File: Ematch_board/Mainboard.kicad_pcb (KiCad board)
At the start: 4 copper layers, 57.3 x 53.3 mm, 128 parts, among them J1 Conn_01x02_Male, J10 Conn_01x02_Male, J2 Conn_01x02_Male, J3 Conn_01x02_Male, J4 Conn_01x02_Male, J5 Conn_01x02_Male, J6 Conn_01x02_Male, J7 Conn_01x06_Female, J8 USB_C_Receptacle_USB2.0, J9 Conn_01x02_Male, Q1 MMDT2222A, Q51 PMV20ENR, Q52 PMV20ENR, Q53 PMV20ENR, Q54 PMV20ENR, Q55 PMV20ENR, Q56 PMV20ENR, U1 LTV-247, U2 LTC4411, U3 RT9025-25GSP, U4 LTC4411, U5 SN65HVD230, U6 CP2102-GMR-QFN28

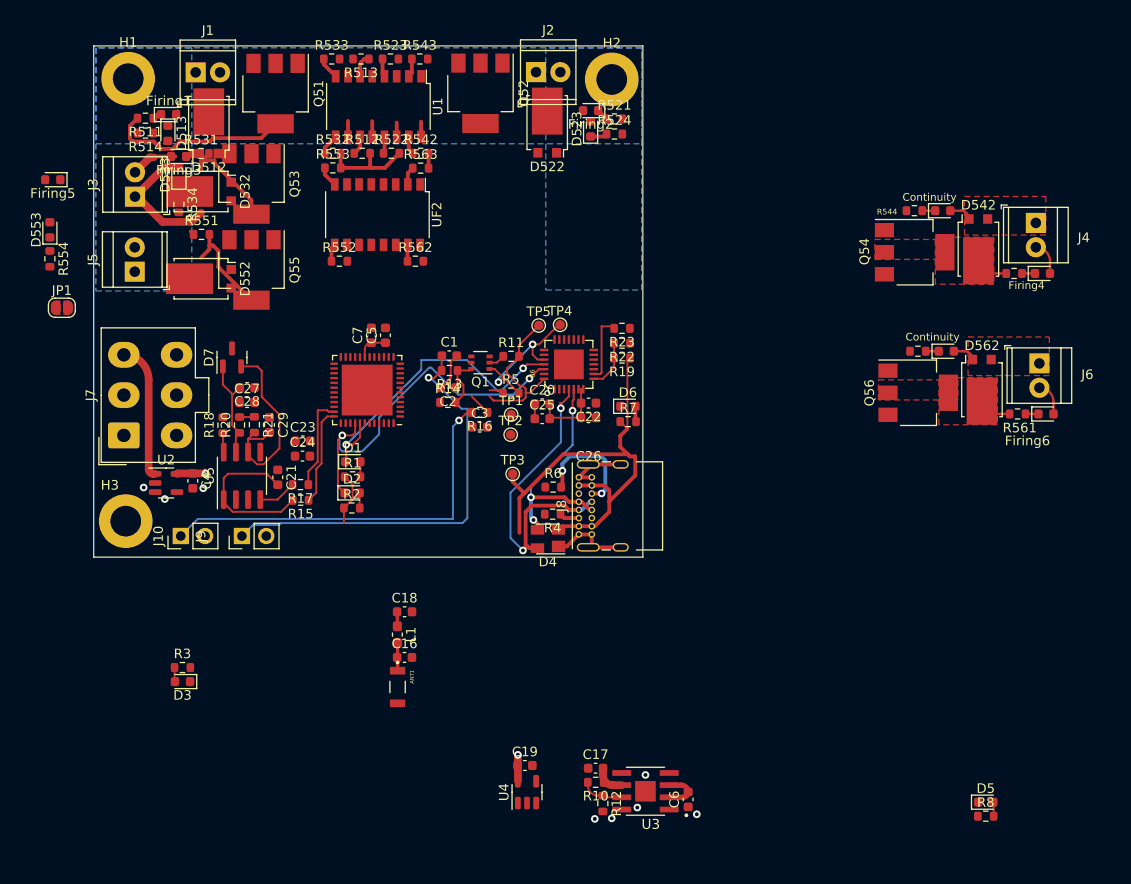
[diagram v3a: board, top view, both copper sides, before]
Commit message: completed layout for screw terminals, moved some LEDs
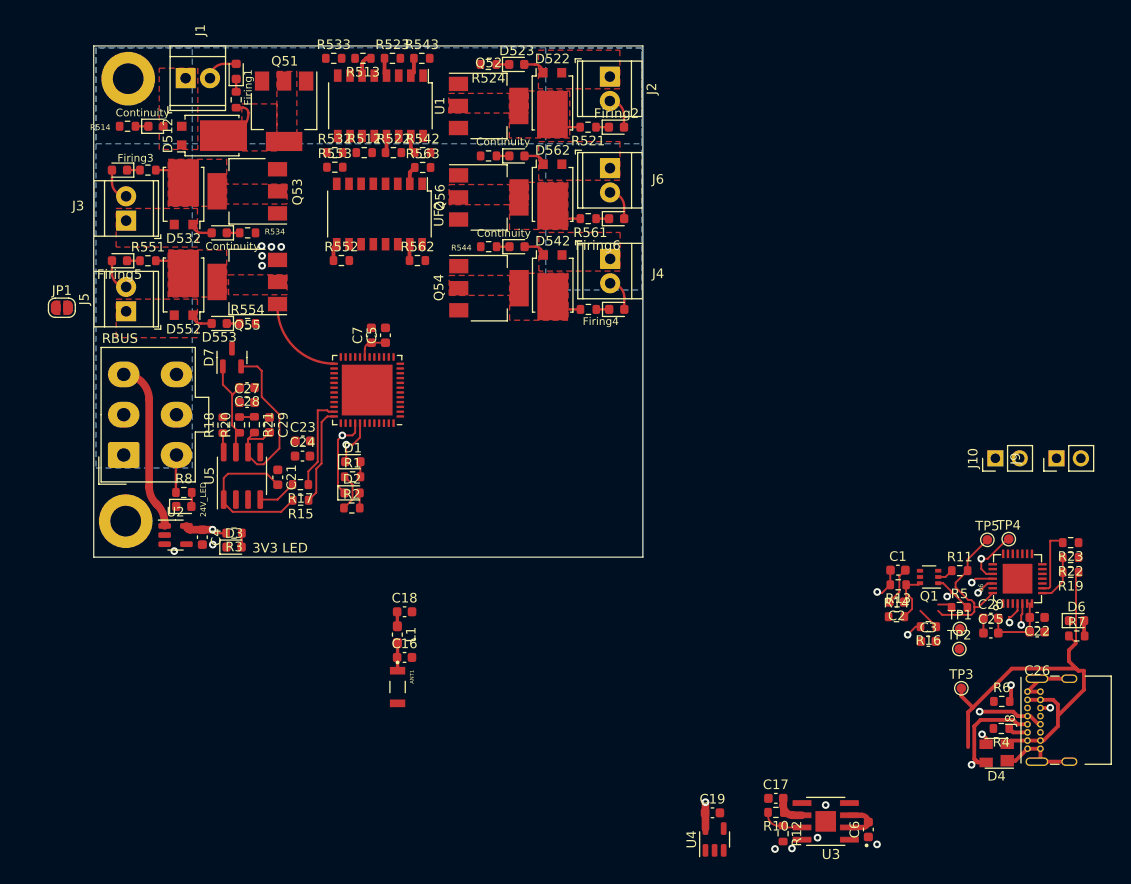
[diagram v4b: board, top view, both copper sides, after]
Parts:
- removed H2: MountingHole_Pad, MountingHole:MountingHole_3.2mm_M3_DIN965_Pad
- D3: value PWR_LED -> 3V3 LED
- J7: value Conn_01x06_Female -> RBUS
- moved R8 90.2 mm to (127.4, 116.1)
- moved D5 89.1 mm to (127.4, 117.5)
- moved J9 85.3 mm to (218.4, 112.5)
- moved J10 85.3 mm to (212.0, 112.5)
- moved D6 51.8 mm to (220.4, 129.4)
- moved R16 51.8 mm to (205.0, 130.1)
- moved R22 51.8 mm to (219.8, 122.8)
- moved R4 51.8 mm to (212.6, 140.7)
- moved C1 51.8 mm to (201.8, 124.2)
- moved C3 51.8 mm to (205.0, 131.6)
- moved Q1 51.8 mm to (205.1, 124.9)
- moved R14 51.8 mm to (201.7, 129.0)
- moved R19 51.8 mm to (219.8, 124.4)
- moved R23 51.8 mm to (219.8, 121.3)
- moved TP2 51.8 mm to (208.2, 132.4)
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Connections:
- D522 pad 3: Net-(D522-Pad3) -> unconnected-(D522-Pad3)
- Firing1 pad 2: /24V -> +24V
- Firing2 pad 2: /24V -> +24V
- Firing3 pad 2: /24V -> +24V
- Firing4 pad 2: /24V -> +24V
- Firing5 pad 2: /24V -> +24V
- Firing6 pad 2: /24V -> +24V
- J1 pad 2: /24V -> +24V
- J2 pad 2: /24V -> +24V
- J3 pad 2: /24V -> +24V
- J4 pad 2: /24V -> +24V
- J5 pad 2: /24V -> +24V
- J6 pad 2: /24V -> +24V
- Q51 pad 1: /ematch/Nuke 1 -> /Nuke 1
- Q52 pad 1: /ematch/Nuke 2 -> /Nuke 2
- Q52 pad 2: Net-(D522-Pad3) -> Net-(Q52-Pad2)
- Q52 pad 4: Net-(D522-Pad3) -> Net-(Q52-Pad2)
- Q53 pad 1: /ematch/Nuke 3 -> /Nuke 3
- Q54 pad 1: /ematch/Nuke 4 -> /Nuke 4
- Q55 pad 1: /ematch/Nuke 5 -> /Nuke 5
- Q56 pad 1: /ematch/Nuke 6 -> /Nuke 6
- R512 pad 1: /ematch/Cont1 -> /Cont 1
- R521 pad 2: Net-(D522-Pad3) -> Net-(Q52-Pad2)
- R522 pad 1: /ematch/Cont2 -> /Cont 2
- R532 pad 1: /ematch/Cont3 -> /Cont 3
- R542 pad 1: /ematch/Cont4 -> /Cont 4
- R552 pad 1: /ematch/Cont5 -> /Cont 5
- R562 pad 1: /ematch/Cont6 -> /Cont 6
- U1 pad 11: /ematch/Cont1 -> /Cont 1
- U1 pad 13: /ematch/Cont2 -> /Cont 2
- U1 pad 15: /ematch/Cont4 -> /Cont 4
- U1 pad 9: /ematch/Cont3 -> /Cont 3
- UF2 pad 15: /ematch/Cont6 -> /Cont 6
- UF2 pad 9: /ematch/Cont5 -> /Cont 5
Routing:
- net Net-(C1-Pad1): track 43.6 -> 2.86 mm
- net Net-(C3-Pad1): track 41.3 -> 1.68 mm
- net /TXD: track 38.8 -> 11.3 mm
- net +24V: track 0.00 -> 25.0 mm
- net /RXD: track 32.3 -> 7.27 mm
- net /Data+: track 33.2 -> 14.0 mm
- net Net-(D512-Pad3): track 19.2 -> 5.42 mm
- net /Data-: track 23.7 -> 10.4 mm
- net /24V: track 12.6 -> 0.00 mm
- net Net-(D532-Pad1): track 14.0 -> 2.42 mm
- net GND: track 32.3 -> 20.9 mm, vias 8 -> 12
- net Net-(Firing3-Pad1): track 11.0 -> 1.35 mm
- net /Nuke 5: track 0.00 -> 9.35 mm
- net Net-(J8-PadB5): track 11.9 -> 2.59 mm
- net Net-(D552-Pad3): track 10.5 -> 3.60 mm
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- added copper zone on B.Cu, net +24V
- added copper zone on F.Cu, net Net-(D512-Pad1)
- added copper zone on F.Cu, net Net-(D512-Pad3)
- added copper zone on F.Cu, net Net-(D522-Pad1)
- added copper zone on F.Cu, net Net-(D532-Pad1)
- added copper zone on F.Cu, net Net-(D532-Pad3)
- added copper zone on F.Cu, net Net-(D552-Pad1)
- added copper zone on F.Cu, net Net-(D552-Pad3)
- added copper zone on F.Cu, net Net-(Q52-Pad2)
- removed copper zone on B.Cu, net /24V

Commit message: initial routing of cont and nuke traces
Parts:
- added H2: MountingHole_Pad, MountingHole:MountingHole_3.2mm_M3_DIN965_Pad, F.Cu at (171.3, 119.0)
- D3: value 3V3 LED -> PWR_LED
- moved R563 3.28 mm to (150.1, 84.6), turned to 180 degrees
- moved R553 2.64 mm to (144.2, 84.6)
- moved R562 2.35 mm to (151.8, 94.2)
- moved UF2 2.35 mm to (147.9, 89.4)
- moved R552 2.31 mm to (144.2, 94.2)
- moved R532 0.80 mm to (143.9, 80.5)
- moved R512 0.68 mm to (146.8, 80.5)
- moved R522 0.59 mm to (149.8, 80.5)
- moved R542 0.50 mm to (152.8, 80.5)
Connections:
- GND1 pad 12: /Nuke 1 -> unconnected-(GND1-Pad12)
- GND1 pad 17: /Cont 4 -> unconnected-(GND1-Pad17)
- GND1 pad 18: /Cont 2 -> unconnected-(GND1-Pad18)
- GND1 pad 20: /Cont 1 -> unconnected-(GND1-Pad20)
- GND1 pad 22: /Cont 3 -> unconnected-(GND1-Pad22)
- GND1 pad 24: /Nuke 3 -> unconnected-(GND1-Pad24)
- GND1 pad 25: /Nuke 5 -> unconnected-(GND1-Pad25)
- GND1 pad 28: unconnected-(GND1-Pad28) -> /Cont 4
- GND1 pad 29: unconnected-(GND1-Pad29) -> /Cont 2
- GND1 pad 30: unconnected-(GND1-Pad30) -> /Cont 1
- GND1 pad 31: unconnected-(GND1-Pad31) -> /Cont 3
- GND1 pad 32: unconnected-(GND1-Pad32) -> /Nuke 1
- GND1 pad 33: unconnected-(GND1-Pad33) -> /Nuke 3
- GND1 pad 34: unconnected-(GND1-Pad34) -> /Nuke 5
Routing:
- net /Nuke 1: track 0.00 -> 35.2 mm
- net /Cont 4: track 1.90 -> 33.8 mm
- net /Cont 2: track 1.62 -> 32.3 mm
- net /Cont 1: track 0.00 -> 30.4 mm
- net /Cont 3: track 0.00 -> 29.8 mm
- net /Nuke 3: track 0.00 -> 29.5 mm
- net /Nuke 2: track 0.00 -> 24.3 mm
- net /Nuke 6: track 0.00 -> 14.4 mm
- net +3V3: track 22.9 -> 37.2 mm, vias 2 -> 3
- net /Nuke 4: track 0.00 -> 8.43 mm
- net /Nuke 5: track 9.35 -> 14.0 mm
- net /Cont 5: track 1.84 -> 4.75 mm
- net Net-(R563-Pad1): track 1.91 -> 0.00 mm
- net Net-(R553-Pad1): track 0.00 -> 1.69 mm
- net /CAN_RX: track 9.92 -> 9.26 mm
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
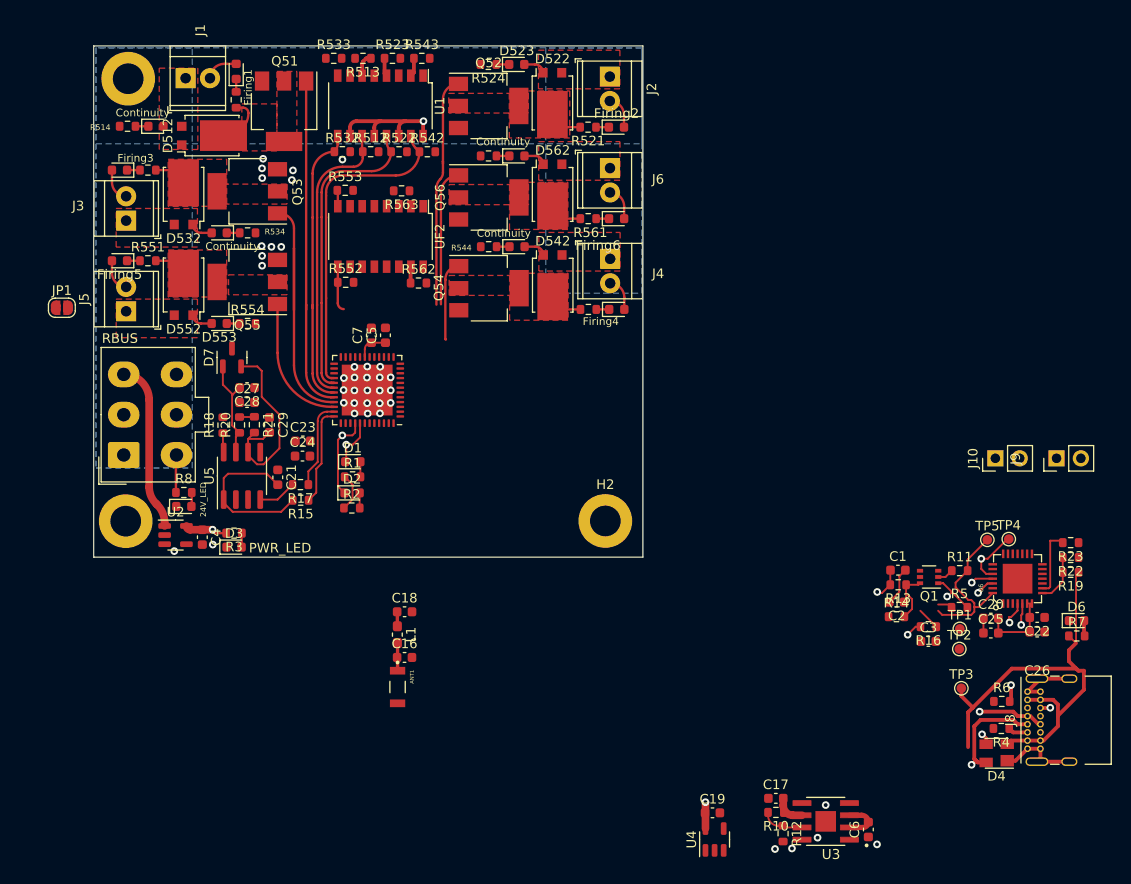
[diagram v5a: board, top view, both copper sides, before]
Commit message: completed routing, changed antenna for U.FL connector
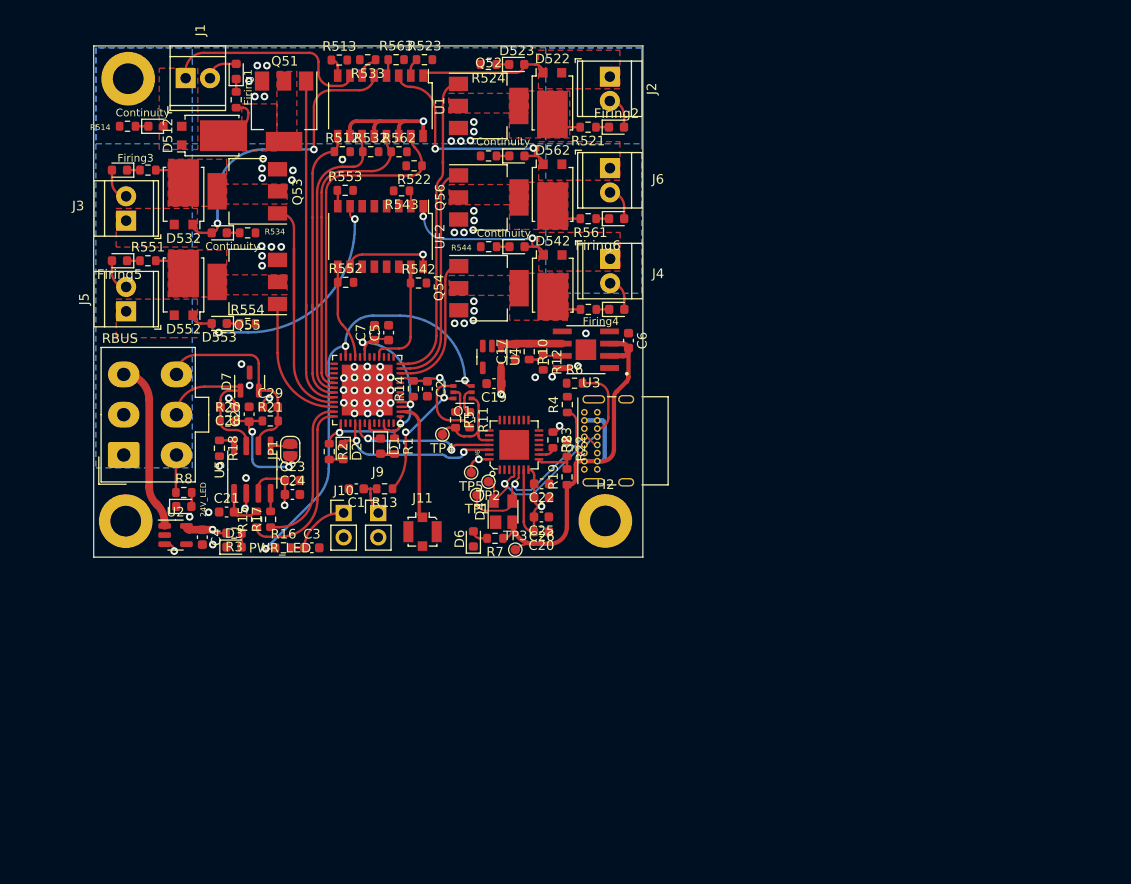
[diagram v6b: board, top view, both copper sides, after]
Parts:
- removed ANT1: AMCA31-2R450G-S1F-T3, iclr:ANT_AMCA31-2R450G-S1F-T3
- removed C16: 33pF, Capacitor_SMD:C_0603_1608Metric
- removed C18: 100pF, Capacitor_SMD:C_0603_1608Metric
- removed L1: LQG15WZ1N8B02D, Inductor_SMD:L_0603_1608Metric_Pad1.05x0.95mm_HandSolder
- added J11: Conn_Coaxial, Connector_Coaxial:U.FL_Molex_MCRF_73412-0110_Vertical, F.Cu at (152.2, 120.2)
- moved J9 70.9 mm to (147.6, 118.2), turned to 0 degrees
- moved J10 68.2 mm to (144.0, 118.2), turned to 0 degrees
- moved R16 67.7 mm to (137.8, 121.8), turned to 0 degrees
- moved C3 65.0 mm to (140.7, 121.8)
- moved D6 63.5 mm to (157.6, 120.9), turned to 90 degrees
- moved R7 61.5 mm to (159.8, 120.8), turned to 180 degrees
- moved TP4 60.1 mm to (154.3, 110.0), turned to 180 degrees
- moved D4 57.3 mm to (160.6, 118.1), turned to 90 degrees
- moved C1 57.1 mm to (145.3, 115.7), turned to 180 degrees
- moved C6 56.8 mm to (173.7, 100.2), turned to -90 degrees
- moved R4 56.5 mm to (167.3, 106.9), turned to 90 degrees
- moved R5 56.1 mm to (155.7, 108.5), turned to -90 degrees
- moved R14 55.7 mm to (151.3, 105.2), turned to 90 degrees
- moved R6 55.5 mm to (168.1, 104.7)
- moved U4 55.4 mm to (159.5, 101.9), turned to -90 degrees
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- renumbered R532 to R512, R533 to R513, R542 to R522, R543 to R523, R512 to R532, R513 to R533, R562 to R542, R563 to R543, R522 to R562, R523 to R563
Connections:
- GND1 pad 10: unconnected-(GND1-Pad10) -> /Nuke 4
- GND1 pad 11: unconnected-(GND1-Pad11) -> /Nuke 6
- GND1 pad 12: unconnected-(GND1-Pad12) -> /Nuke 2
- GND1 pad 13: /Nuke 6 -> unconnected-(GND1-Pad13)
- GND1 pad 14: /Nuke 4 -> unconnected-(GND1-Pad14)
- GND1 pad 15: /Nuke 2 -> unconnected-(GND1-Pad15)
- GND1 pad 16: /Cont 6 -> /Cont 4
- GND1 pad 28: /Cont 4 -> /Cont 2
- GND1 pad 29: /Cont 2 -> /Cont 6
- GND1 pad 30: /Cont 1 -> /Cont 3
- GND1 pad 31: /Cont 3 -> /Cont 1
- R512 pad 1: /Cont 3 -> /Cont 1
- R522 pad 1: /Cont 4 -> /Cont 2
- R532 pad 1: /Cont 1 -> /Cont 3
- R542 pad 1: /Cont 6 -> /Cont 4
- R562 pad 1: /Cont 2 -> /Cont 6
- U1 pad 1: Net-(D542-Pad1) -> Net-(D522-Pad1)
- U1 pad 11: /Cont 1 -> /Cont 3
- U1 pad 13: /Cont 2 -> /Cont 6
- U1 pad 15: /Cont 4 -> /Cont 2
- U1 pad 3: Net-(D522-Pad1) -> Net-(D562-Pad1)
- U1 pad 5: Net-(D512-Pad1) -> Net-(D532-Pad1)
- U1 pad 7: Net-(D532-Pad1) -> Net-(D512-Pad1)
- U1 pad 9: /Cont 3 -> /Cont 1
- UF2 pad 1: Net-(D562-Pad1) -> Net-(D542-Pad1)
- UF2 pad 15: /Cont 6 -> /Cont 4
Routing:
- net +3V3: track 37.2 -> 90.2 mm, vias 3 -> 11
- net /BOOT: track 2.35 -> 45.7 mm, vias 0 -> 3
- net /Cont 6: track 1.67 -> 32.3 mm
- net Net-(D532-Pad1): track 2.42 -> 31.7 mm, vias 0 -> 2
- net Net-(D552-Pad1): track 2.42 -> 26.1 mm, vias 0 -> 2
- net /Cont 4: track 33.8 -> 11.9 mm
- net Net-(D512-Pad1): track 0.00 -> 21.9 mm
- net Net-(D562-Pad1): track 2.42 -> 23.3 mm, vias 0 -> 2
- net Net-(D542-Pad1): track 2.42 -> 18.6 mm, vias 0 -> 2
- net GND: track 20.9 -> 5.62 mm, vias 39 -> 67
- net /EN: track 6.16 -> 19.4 mm, vias 0 -> 3
- net Net-(C21-Pad2): track 16.6 -> 4.78 mm
- net /LNA_IN: track 1.52 -> 13.0 mm
- net Net-(D522-Pad1): track 2.42 -> 13.6 mm
- net /Vref: track 1.52 -> 12.3 mm, vias 0 -> 2
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
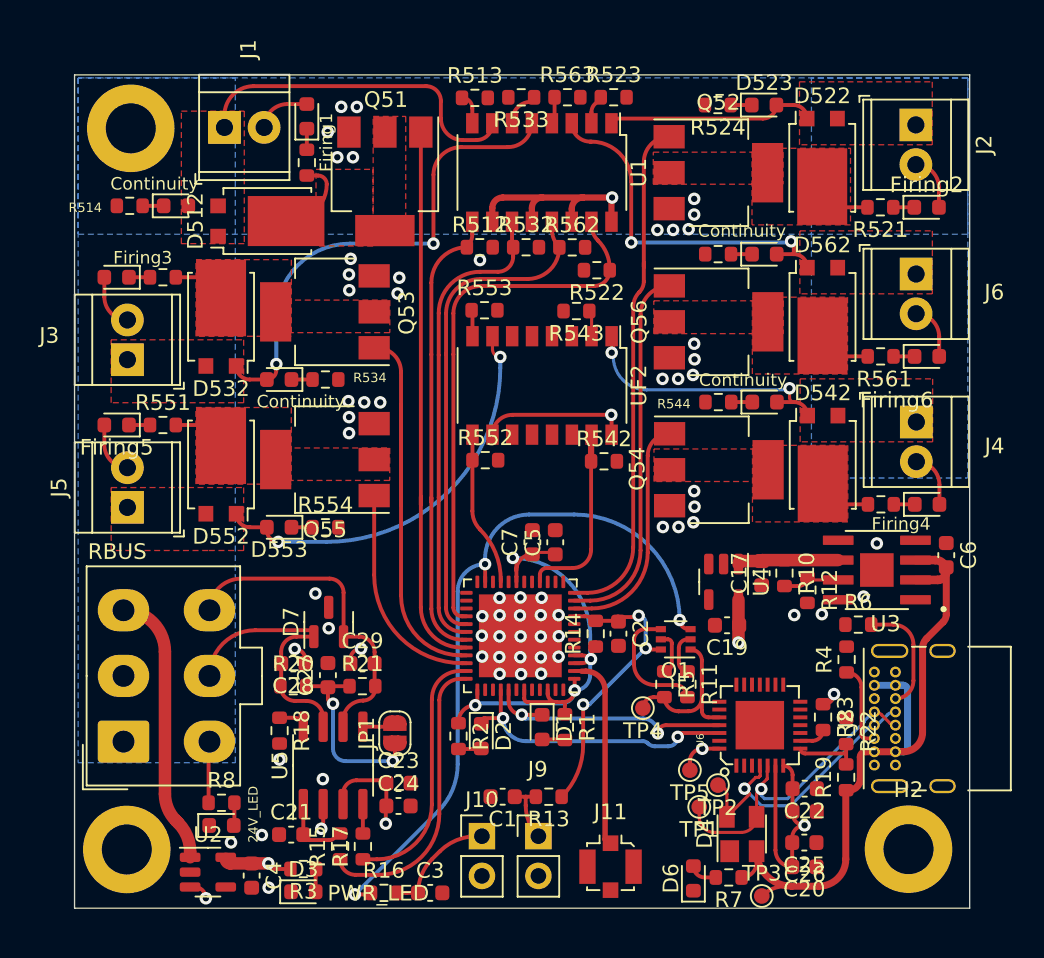
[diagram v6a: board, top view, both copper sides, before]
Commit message: created GND planes and fixed zone priority to prevent shorting nets
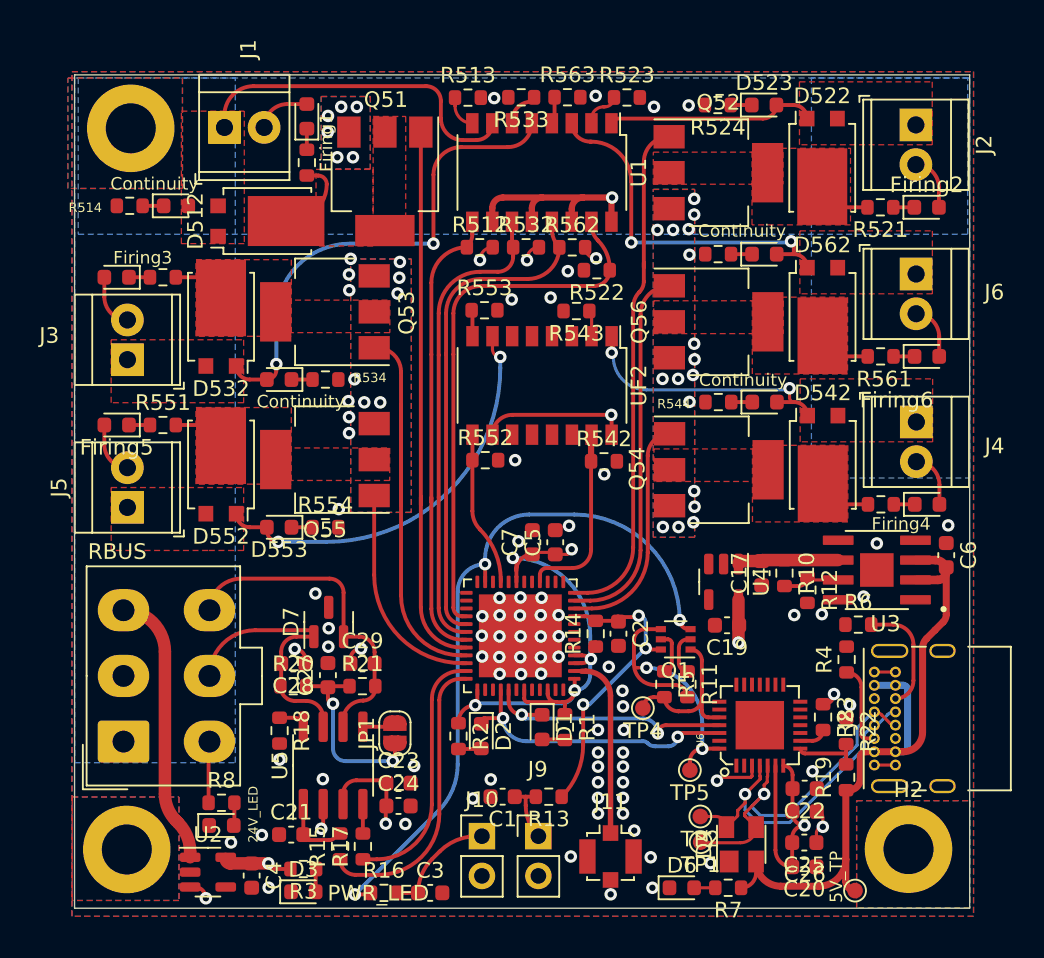
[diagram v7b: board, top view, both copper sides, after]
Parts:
- moved TP3 5.97 mm to (167.9, 121.7)
- moved TP2 2.30 mm to (158.0, 116.9)
- moved TP1 2.26 mm to (158.0, 118.6)
- moved D6 0.95 mm to (156.8, 121.5), turned to 0 degrees
- moved R523 0.85 mm to (153.3, 71.0)
- moved R7 0.66 mm to (159.8, 121.5)
- moved D4 0.66 mm to (160.6, 118.7)
- moved J11 0.65 mm to (152.2, 119.5)
- moved R513 0.45 mm to (143.1, 71.0)
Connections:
- D522 pad 3: unconnected-(D522-Pad3) -> Net-(D522-Pad3)
- Q52 pad 2: Net-(Q52-Pad2) -> Net-(D522-Pad3)
- Q52 pad 4: Net-(Q52-Pad2) -> Net-(D522-Pad3)
- R521 pad 2: Net-(Q52-Pad2) -> Net-(D522-Pad3)
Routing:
- net GND: track 5.62 -> 18.4 mm, vias 67 -> 117
- net /DTR: track 11.0 -> 19.0 mm, vias 1 -> 2
- net unconnected-(D522-Pad3): track 3.60 -> 0.00 mm
- net Net-(D522-Pad3): track 0.00 -> 3.60 mm
- net /Data-: track 20.7 -> 23.5 mm
- net /Data+: track 19.4 -> 21.9 mm
- net +3V3: track 90.2 -> 91.4 mm, vias 11 -> 12
- net VBUS: track 47.4 -> 46.6 mm
- net /LNA_IN: track 13.0 -> 12.2 mm
- net Net-(D6-Pad2): track 1.90 -> 1.36 mm
- added copper zone on B.Cu, net GND
- added copper zone on F.Cu, net GND
- added copper zone on F.Cu, net Net-(D522-Pad3)
- removed copper zone on F.Cu, net Net-(Q52-Pad2)
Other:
- board text added: "5V_TP"
